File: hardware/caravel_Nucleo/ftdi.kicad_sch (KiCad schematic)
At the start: 28 parts, among them J2 M20-9990246, U1 FT232HQ, U11 TAR5S33UTE85LF, Y1 ABM8G-12.000MHZ-18-D2Y-T

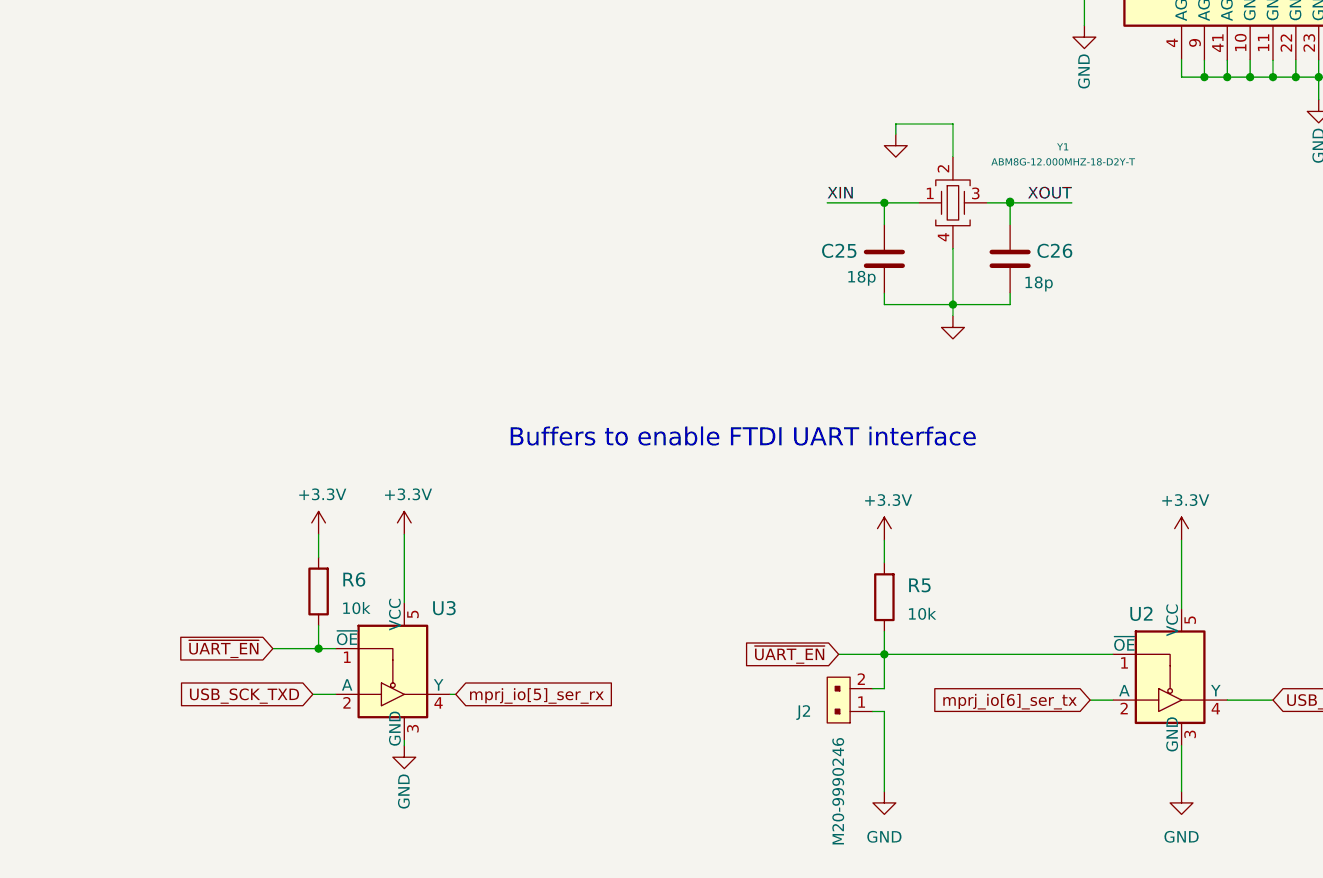
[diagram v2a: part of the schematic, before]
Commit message: Move components to local library
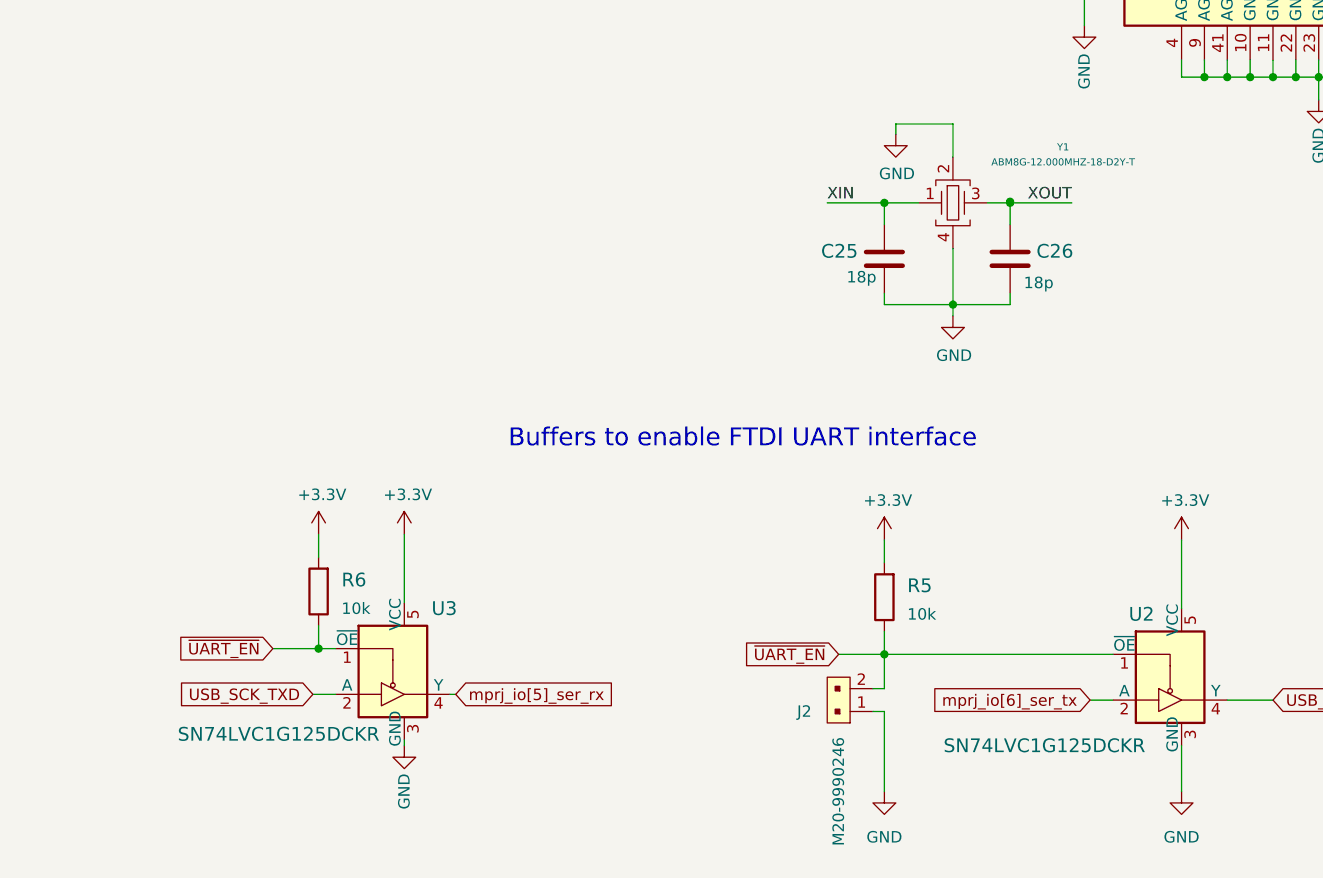
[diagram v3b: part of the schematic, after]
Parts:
- C1, C23: footprint antmicro-footprints:0805-cap -> caravel_Nucleo-footprints:0805-cap; symbol antmicroCapacitorsmisc:C_10n_0805 -> caravel_Nucleo:C_10n_0805
- C2, C3, C4, C5, C6, C7, C8: footprint antmicro-footprints:0603-cap -> caravel_Nucleo-footprints:0603-cap; symbol antmicroCapacitors0603:C_100n_0603 -> caravel_Nucleo:C_100n_0603
- C22: footprint antmicro-footprints:0805-cap -> caravel_Nucleo-footprints:0805-cap; symbol antmicroCapacitorsmisc:C_1u_0805 -> caravel_Nucleo:C_1u_0805
- C24: footprint antmicro-footprints:0805-cap -> caravel_Nucleo-footprints:0805-cap; symbol antmicroCapacitorsmisc:C_10u_0805 -> caravel_Nucleo:C_10u_0805
- C25, C26: value (none) -> C_18p_0603; footprint (none) -> caravel_Nucleo-footprints:0603-cap; symbol antmicroCapacitors0603:C_18p_0603 -> caravel_Nucleo:C_18p_0603
- D1, D2: footprint antmicro-footprints:LED0603_GREEN -> caravel_Nucleo-footprints:LED0603_GREEN; symbol antmicroLEDIndicationDiscrete:KP-1608CGCK_GREEN -> caravel_Nucleo:KP-1608CGCK_GREEN
- J2: footprint antmicro-footprints:PinHeader_1x2_P2.54mm -> caravel_Nucleo-footprints:PinHeader_1x2_P2.54mm; symbol antmicroRectangularConnectorsHeadersMalePins:M20-9990246 -> caravel_Nucleo:M20-9990246
- R1, R28, R5, R6: footprint antmicro-footprints:0603-res -> caravel_Nucleo-footprints:0603-res; symbol antmicroResistors0603:R_10k_0603 -> caravel_Nucleo:R_10k_0603
- R2: footprint antmicro-footprints:0603-res -> caravel_Nucleo-footprints:0603-res; symbol antmicroResistors0603:R_12k_1%_0603 -> caravel_Nucleo:R_12k_1%_0603
- R3, R4: footprint antmicro-footprints:0603-res -> caravel_Nucleo-footprints:0603-res; symbol antmicroResistors0603:R_150R_0603 -> caravel_Nucleo:R_150R_0603
- U1: footprint antmicro-footprints:QFN-48-1EP_6x6mm -> caravel_Nucleo-footprints:QFN-48-1EP_6x6mm; symbol antmicroInterfaceControllers:FT232HQ -> caravel_Nucleo:FT232HQ
- U11: footprint antmicro-footprints:SOT-353 -> caravel_Nucleo-footprints:SOT-353; symbol antmicroPMICVoltageRegulatorsLinear:TAR5S33UTE85LF -> caravel_Nucleo:TAR5S33UTE85LF
- U2, U3: value (none) -> SN74LVC1G125DCKR; footprint (none) -> caravel_Nucleo-footprints:SOT-353; symbol antmicroLogicBuffersDriversReceiversTransceivers:SN74LVC1G125DCKR -> caravel_Nucleo:SN74LVC1G125DCKR
- Y1: footprint antmicro-footprints:KX-7 -> caravel_Nucleo-footprints:KX-7; symbol antmicroCrystals:ABM8G-12.000MHZ-18-D2Y-T -> caravel_Nucleo:ABM8G-12.000MHZ-18-D2Y-T

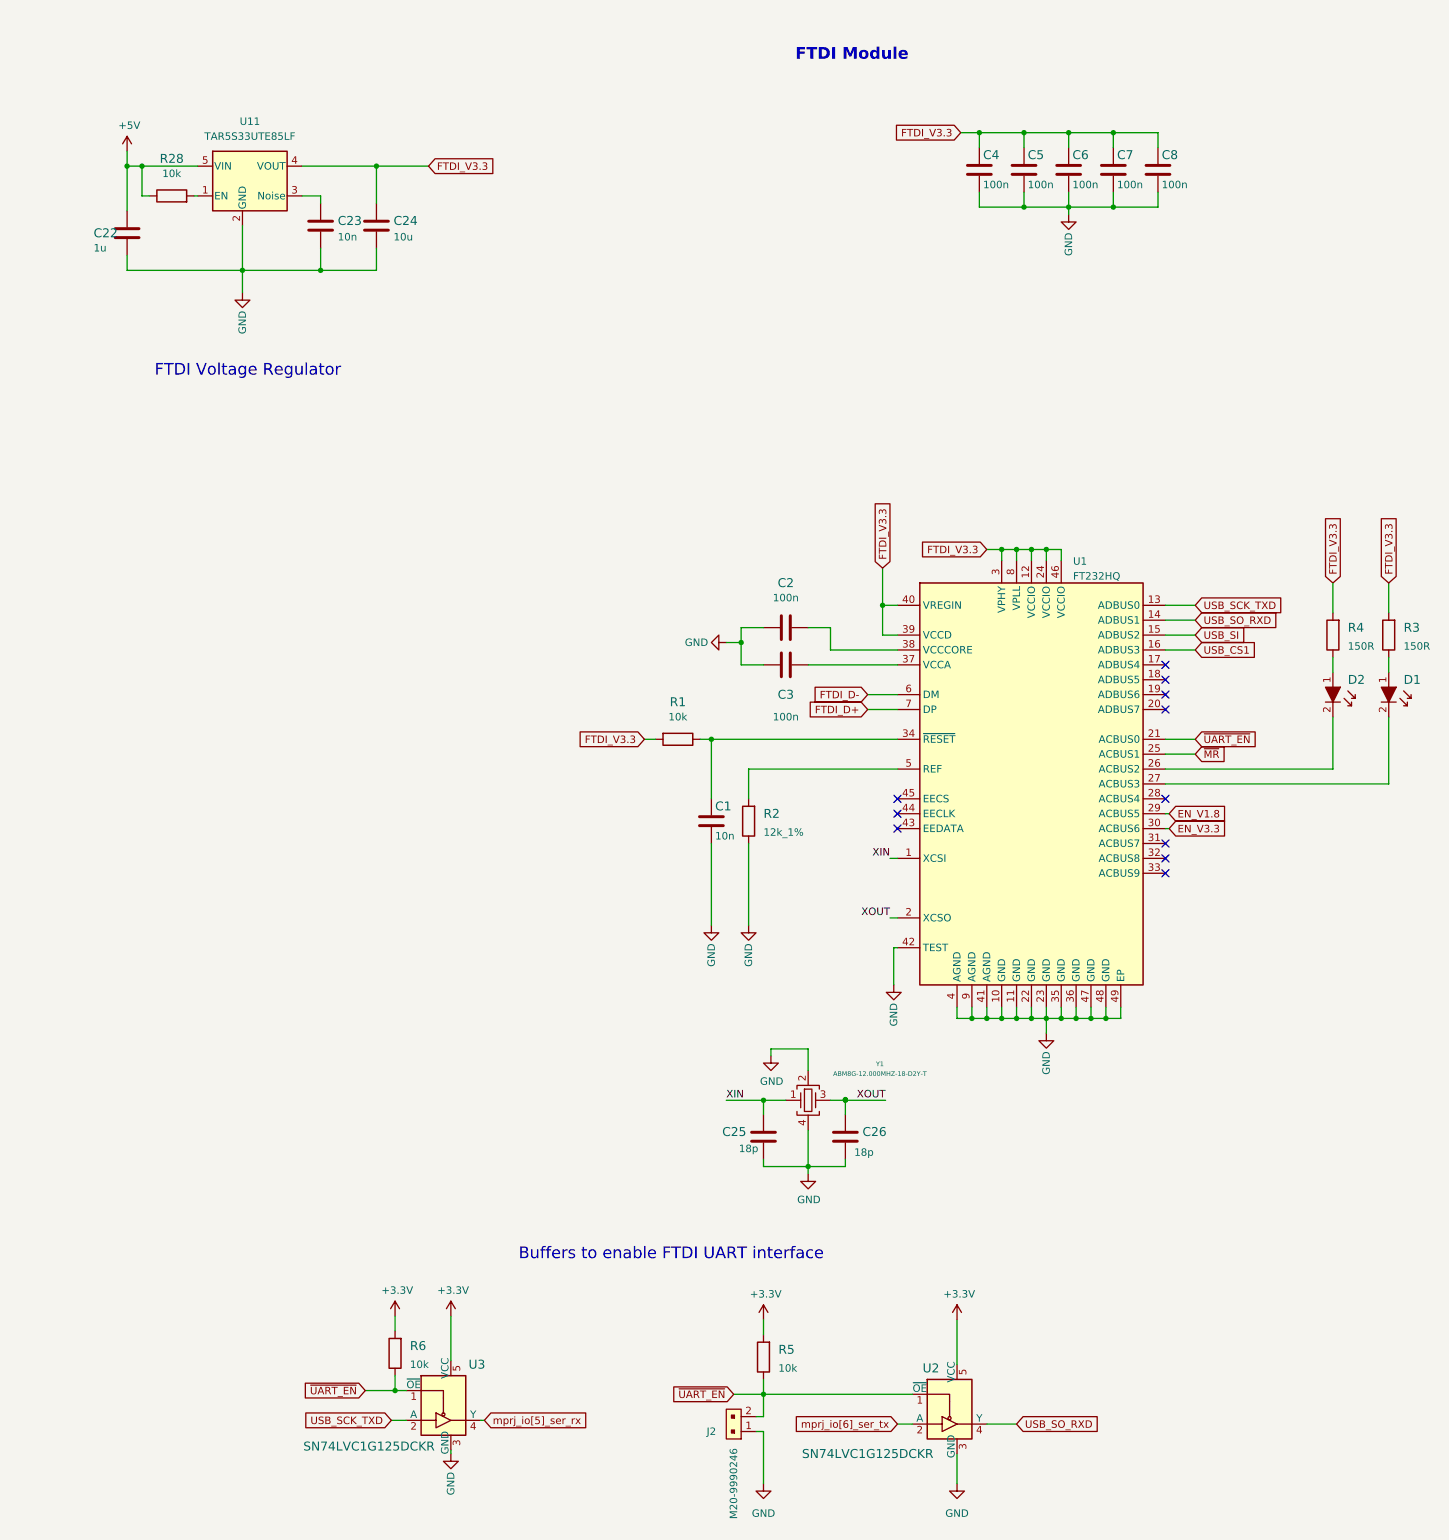
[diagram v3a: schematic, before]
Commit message: Rework FTDI sheet, begin improving main schematic sheet
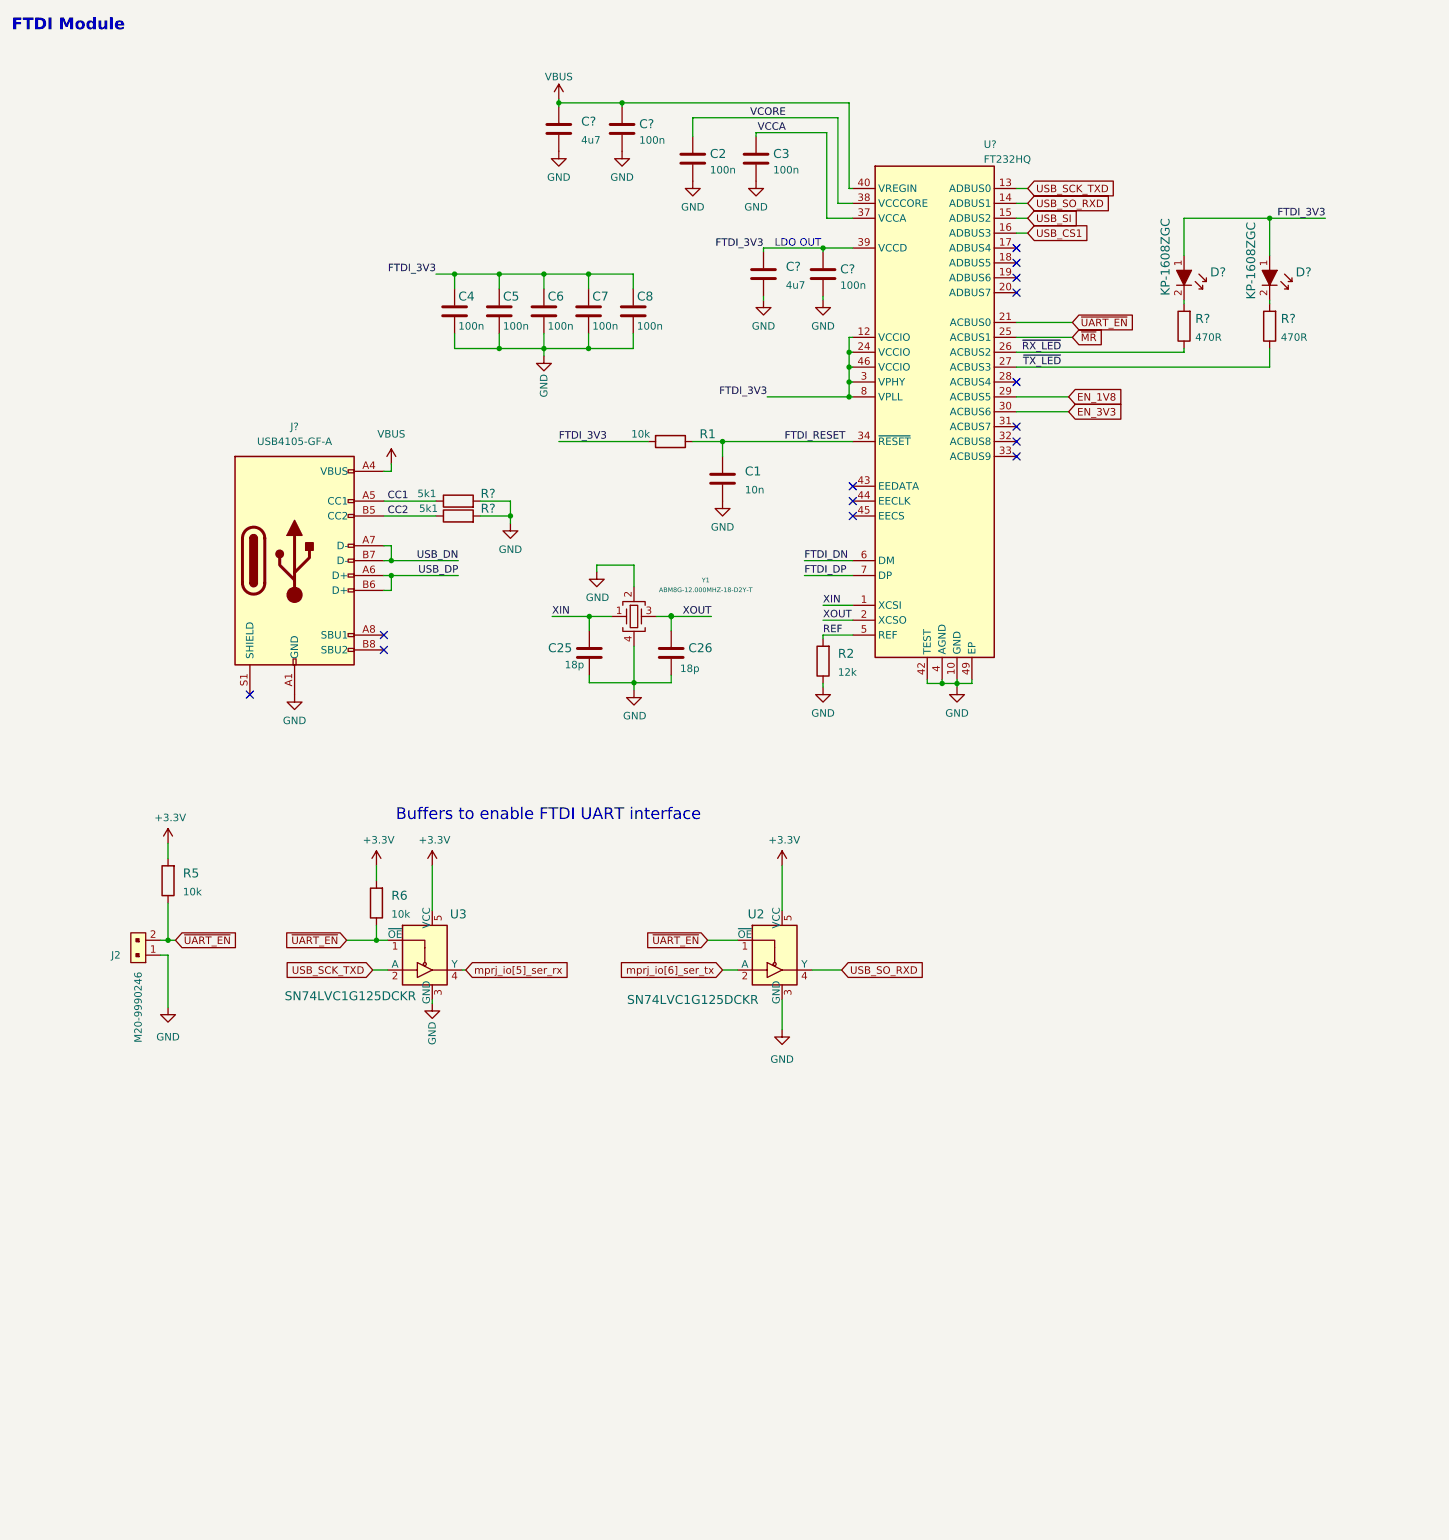
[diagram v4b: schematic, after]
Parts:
- removed C1, C23: C_10n_0805, caravel_Nucleo-footprints:0805-cap, symbol caravel_Nucleo:C_10n_0805
- removed C22: C_1u_0805, caravel_Nucleo-footprints:0805-cap, symbol caravel_Nucleo:C_1u_0805
- removed C24: C_10u_0805, caravel_Nucleo-footprints:0805-cap, symbol caravel_Nucleo:C_10u_0805
- removed D1, D2: KP-1608CGCK_GREEN, caravel_Nucleo-footprints:LED0603_GREEN, symbol caravel_Nucleo:KP-1608CGCK_GREEN
- removed R1, R28: R_10k_0603, caravel_Nucleo-footprints:0603-res, symbol caravel_Nucleo:R_10k_0603
- removed R2: R_12k_1%_0603, caravel_Nucleo-footprints:0603-res, symbol caravel_Nucleo:R_12k_1%_0603
- removed R3, R4: R_150R_0603, caravel_Nucleo-footprints:0603-res, symbol caravel_Nucleo:R_150R_0603
- removed U1: FT232HQ, caravel_Nucleo-footprints:QFN-48-1EP_6x6mm, symbol caravel_Nucleo:FT232HQ
- removed U11: TAR5S33UTE85LF, caravel_Nucleo-footprints:SOT-353, symbol caravel_Nucleo:TAR5S33UTE85LF
- added C1: C_10n_0402, antmicro-footprints:0402-cap, symbol antmicroCapacitors0402:C_10n_0402
- added C? (x2): C_100n_0603, antmicro-footprints:0603-cap, symbol antmicroCapacitors0603:C_100n_0603
- added C? (x2): C_4u7_0603, antmicro-footprints:0603-cap, symbol antmicroCapacitors0603:C_4u7_0603
- added D? (x2): KP-1608ZGC, antmicro-footprints:LED_0603, symbol antmicroLEDIndicationDiscrete:KP-1608ZGC
- added J?: USB4105-GF-A, antmicro-footprints:GCT_USB4105-GF-A, symbol antmicroUSBDVIHDMIConnectors:USB4105-GF-A
- added R1: R_10k_0402, antmicro-footprints:0402-res, symbol antmicroResistors0402:R_10k_0402
- added R2: R_12k_0402, antmicro-footprints:0402-res, symbol antmicroResistors0402:R_12k_0402
- added R? (x2): R_470R_0603, antmicro-footprints:0603-res, symbol antmicroResistors0603:R_470R_0603
- added R? (x2): R_5k1_0402, antmicro-footprints:0402-res, symbol antmicroResistors0402:R_5k1_0402
- added U?: FT232HQ, antmicro-footprints:QFN-48-1EP_6x6mm, symbol antmicroInterfaceControllers:FT232HQ
- C2, C3, C4, C5, C6, C7, C8: footprint caravel_Nucleo-footprints:0603-cap -> antmicro-footprints:0603-cap; symbol caravel_Nucleo:C_100n_0603 -> antmicroCapacitors0603:C_100n_0603
- C25, C26: footprint caravel_Nucleo-footprints:0603-cap -> antmicro-footprints:0603-cap; symbol caravel_Nucleo:C_18p_0603 -> antmicroCapacitors0603:C_18p_0603
- J2: footprint caravel_Nucleo-footprints:PinHeader_1x2_P2.54mm -> antmicro-footprints:PinHeader_1x2_P2.54mm; symbol caravel_Nucleo:M20-9990246 -> antmicroRectangularConnectorsHeadersMalePins:M20-9990246
- R5, R6: footprint caravel_Nucleo-footprints:0603-res -> antmicro-footprints:0603-res; symbol caravel_Nucleo:R_10k_0603 -> antmicroResistors0603:R_10k_0603
- U2, U3: footprint caravel_Nucleo-footprints:SOT-353 -> antmicro-footprints:SOT-353; symbol caravel_Nucleo:SN74LVC1G125DCKR -> antmicroLogicBuffersDriversReceiversTransceivers:SN74LVC1G125DCKR
- Y1: footprint caravel_Nucleo-footprints:KX-7 -> antmicro-footprints:KX-7; symbol caravel_Nucleo:ABM8G-12.000MHZ-18-D2Y-T -> antmicroCrystals:ABM8G-12.000MHZ-18-D2Y-T
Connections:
- net USB_CS1: now also U?.16 (ADBUS3)
- net USB_SCK_TXD: now also U?.13 (ADBUS0)
- net USB_SI: now also U?.15 (ADBUS2)
- net USB_SO_RXD: now also U?.14 (ADBUS1)
- net XIN: now also U?.1 (XCSI)
- net XOUT: now also U?.2 (XCSO)
- net ~{MR}: now also U?.25 (ACBUS1)
- net ~{UART_EN}: now also U?.21 (ACBUS0)
- net VCCA: now reaches C3.2
- net VCCA: now also U?.37 (VCCA)
- net VCORE: now reaches C2.2
- net VCORE: now also U?.38 (VCCCORE)
- net FTDI_V3.3 renamed FTDI_3V3
- net FTDI_3V3: now also C?.1, C?.2, D?.1, D?.1, R1.2, U?.12 (VCCIO), U?.24 (VCCIO), U?.3 (VPHY), U?.39 (VCCD), U?.46 (VCCIO), U?.8 (VPLL)
- net GND renamed AGND
- net AGND: now also C1.2, C?.1, C?.1, C?.2, C?.2, J?.A1 (GND), J?.A12 (GND), J?.B1 (GND), J?.B12 (GND), R2.1, R?.2, R?.2, U?.10 (GND), U?.11 (GND), U?.22 (GND), U?.23 (GND), U?.35 (GND), U?.36 (GND), U?.4 (AGND), U?.41 (AGND), U?.42 (TEST), U?.47 (GND), U?.48 (GND), U?.49 (EP), U?.9 (AGND)
- new net: D?.2, R?.2 (x2)
- new net CC1: J?.A5 (CC1), R?.1
- new net CC2: J?.B5 (CC2), R?.1
- new net EN_1V8: U?.29 (ACBUS5)
- new net EN_3V3: U?.30 (ACBUS6)
- new net FTDI_DN: U?.6 (DM)
- new net FTDI_DP: U?.7 (DP)
- new net FTDI_RESET: C1.1, R1.1, U?.34 (~{RESET})
- new net REF: R2.2, U?.5 (REF)
- new net USB_DN: J?.A7 (D-), J?.B7 (D-)
- new net USB_DP: J?.A6 (D+), J?.B6 (D+)
- new net VBUS: C?.1, C?.2, J?.A4 (VBUS), J?.A9 (VBUS), J?.B4 (VBUS), J?.B9 (VBUS), U?.40 (VREGIN)
- new net ~{RX_LED}: R?.1, U?.26 (ACBUS2)
- new net ~{TX_LED}: R?.1, U?.27 (ACBUS3)
- no-connect marks 11 -> 14
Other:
- note added: "LDO OUT"
- note removed: "FTDI Voltage Regulator"
- moved on the sheet: C2, C25, C26, C3, C4, C5, C6, C7, C8, J2, R5, R6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
